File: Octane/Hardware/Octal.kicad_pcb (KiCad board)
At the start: 2 copper layers, 40 x 109 mm, 136 parts, among them J1 WQP-PJ301M-12_JACK, J10 WQP-PJ301M-12_JACK, J11 WQP-PJ301M-12_JACK, J12 WQP-PJ301M-12_JACK, J13 WQP-PJ301M-12_JACK, J14 WQP-PJ301M-12_JACK, J15 WQP-PJ301M-12_JACK, J16 WQP-PJ301M-12_JACK, J17 EURORACK CONNECTOR, J2 WQP-PJ301M-12_JACK, J3 WQP-PJ301M-12_JACK, J4 WQP-PJ301M-12_JACK, J5 WQP-PJ301M-12_JACK, J6 WQP-PJ301M-12_JACK, J7 WQP-PJ301M-12_JACK, J8 WQP-PJ301M-12_JACK, J9 WQP-PJ301M-12_JACK, U1 TL074, U2 TL074, U3 TL074, U4 TL074, U5 TL074, U6 TL074, U7 LM4040DBZ-10

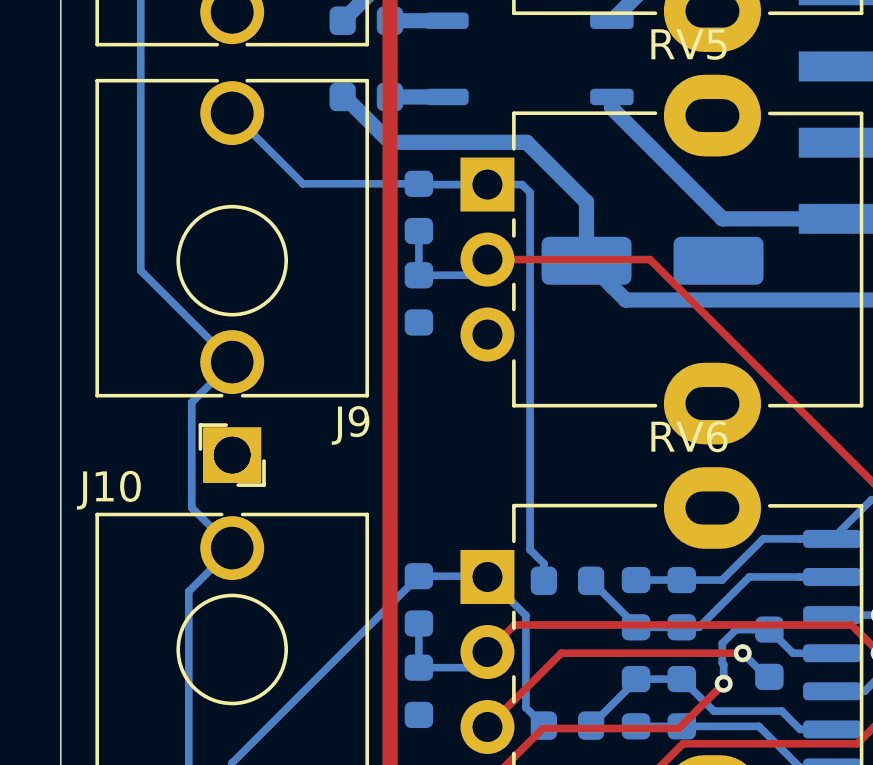
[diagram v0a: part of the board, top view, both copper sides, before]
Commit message: Fixed overlapping trace with pad of C17
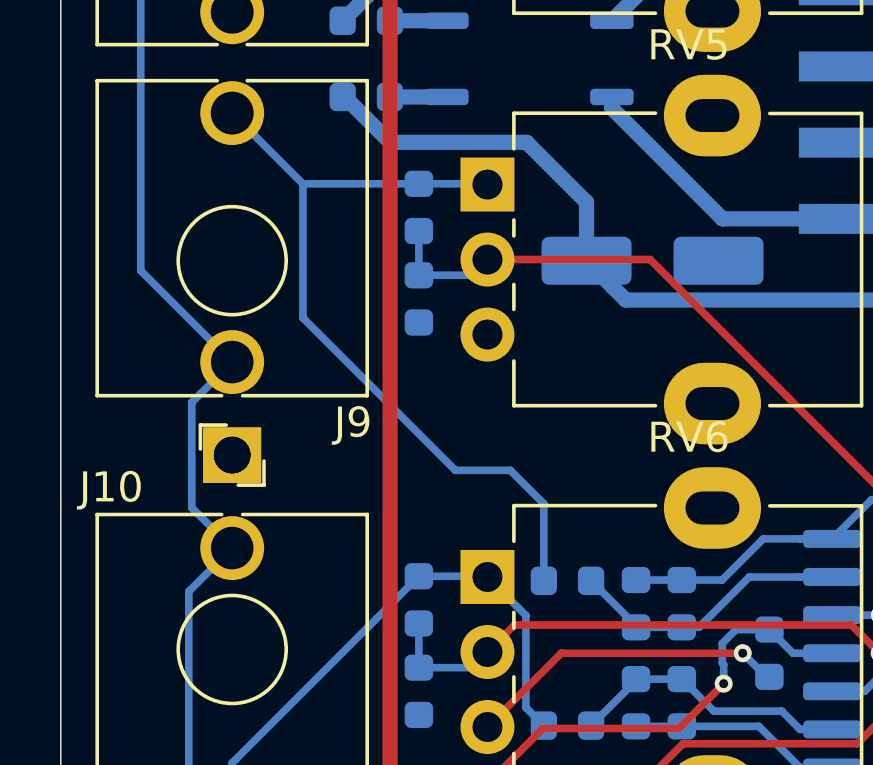
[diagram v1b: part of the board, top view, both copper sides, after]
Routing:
- net Net-(J9-Pad3): track 24.2 -> 27.1 mm
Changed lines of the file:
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@@
     (thickness 1.6)
     (drawings 17)
-    (tracks 996)
+    (tracks 995)
     (zones 0)
     (modules 136)
@@
   (segment (start 173.8075 103.2255) (end 177.673 103.2255) (width 0.254) (layer B.Cu) (net 70))
   (segment (start 171.45 100.868) (end 173.8075 103.2255) (width 0.254) (layer B.Cu) (net 70))
-  (segment (start 177.6985 103.251) (end 177.673 103.2255) (width 0.254) (layer B.Cu) (net 70))
-  (segment (start 179.959 103.251) (end 177.6985 103.251) (width 0.254) (layer B.Cu) (net 70))
-  (segment (start 181.8385 115.884) (end 181.8385 116.459) (width 0.254) (layer B.Cu) (net 70))
-  (segment (start 181.37999 115.42549) (end 181.8385 115.884) (width 0.254) (layer B.Cu) (net 70))
-  (segment (start 181.37999 103.51799) (end 181.37999 115.42549) (width 0.254) (layer B.Cu) (net 70))
-  (segment (start 181.113 103.251) (end 181.37999 103.51799) (width 0.254) (layer B.Cu) (net 70))
-  (segment (start 179.959 103.251) (end 181.113 103.251) (width 0.254) (layer B.Cu) (net 70))
+  (segment (start 177.673 103.2255) (end 179.959 103.2255) (width 0.254) (layer B.Cu) (net 70))
+  (segment (start 173.8075 107.694698) (end 178.888802 112.776) (width 0.254) (layer B.Cu) (net 70))
+  (segment (start 173.8075 103.2255) (end 173.8075 107.694698) (width 0.254) (layer B.Cu) (net 70))
+  (segment (start 178.888802 112.776) (end 180.721 112.776) (width 0.254) (layer B.Cu) (net 70))
+  (segment (start 181.8385 113.8935) (end 181.8385 116.459) (width 0.254) (layer B.Cu) (net 70))
+  (segment (start 180.721 112.776) (end 181.8385 113.8935) (width 0.254) (layer B.Cu) (net 70))
   (segment (start 181.240001 117.613001) (end 179.959 116.332) (width 0.254) (layer B.Cu) (net 71))
   (segment (start 181.240001 120.686501) (end 181.240001 117.613001) (width 0.254) (layer B.Cu) (net 71))
